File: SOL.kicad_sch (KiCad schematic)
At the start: 4 parts, among them J2 Conn_Coaxial, J3 Conn_Coaxial, J4 Conn_Coaxial

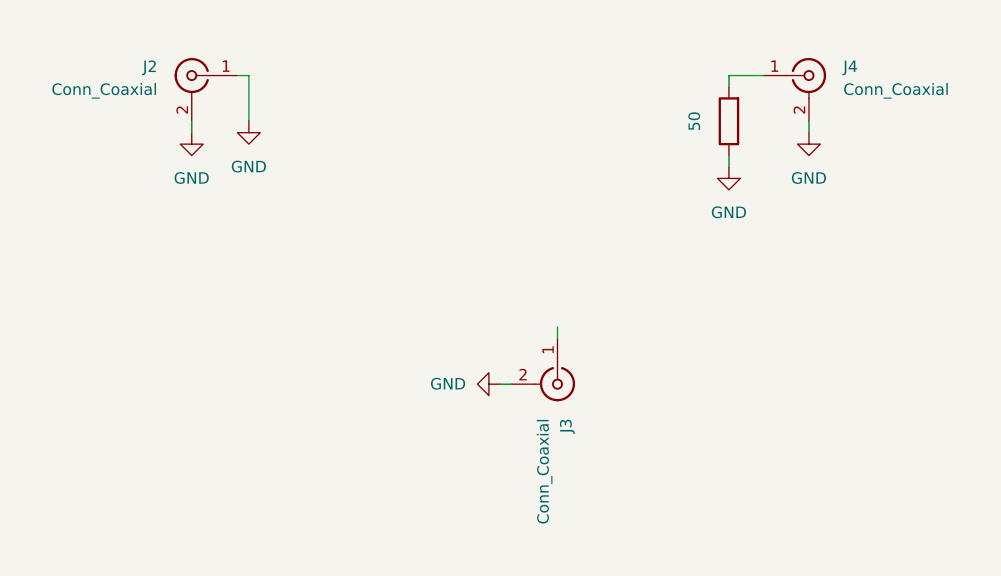
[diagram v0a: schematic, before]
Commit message: used altium files to build kicad models of mm5800 and started new twpatron
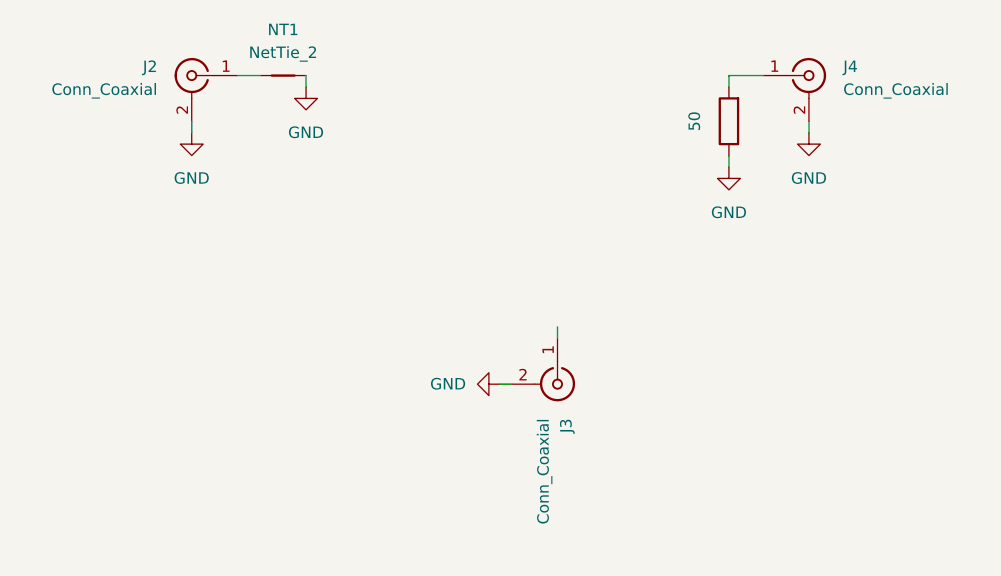
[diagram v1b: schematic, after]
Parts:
- added NT1: NetTie_2, Jumper:SolderJumper-2_P1.3mm_Bridged_Pad1.0x1.5mm, symbol Device:NetTie_2
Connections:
- net GND: now also NT1.2; no longer J2.1 (In)
- new net: J2.1 (In), NT1.1
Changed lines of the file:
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@@
 	(wire
 		(pts
-			(xy 97.79 73.66) (xy 97.79 78.74)
+			(xy 104.14 74.93) (xy 104.14 73.66)
 		)
 		(stroke
@@
 	(wire
 		(pts
-			(xy 96.52 73.66) (xy 97.79 73.66)
+			(xy 96.52 73.66) (xy 99.06 73.66)
 		)
 		(stroke
@@
 	)
 	(symbol
+		(lib_id "Device:NetTie_2")
+		(at 101.6 73.66 0)
+		(unit 1)
+		(exclude_from_sim no)
+		(in_bom no)
+		(on_board yes)
+		(dnp no)
+		(fields_autoplaced yes)
+		(property "Reference" "NT1"
+			(at 101.6 68.58 0)
+			(effects
+				(font
+					(size 1.27 1.27)
+				)
+			)
+		)
+		(property "Value" "NetTie_2"
+			(at 101.6 71.12 0)
+			(effects
+				(font
+					(size 1.27 1.27)
+				)
+			)
+		)
+		(property "Footprint" "Jumper:SolderJumper-2_P1.3mm_Bridged_Pad1.0x1.5mm"
+			(at 101.6 73.66 0)
+			(effects
+				(font
+					(size 1.27 1.27)
+				)
+				(hide yes)
+			)
+		)
+		(property "Datasheet" "~"
+			(at 101.6 73.66 0)
+			(effects
+				(font
+					(size 1.27 1.27)
+				)
+				(hide yes)
+			)
+		)
+		(property "Description" "Net tie, 2 pins"
+			(at 101.6 73.66 0)
+			(effects
+				(font
+					(size 1.27 1.27)
+				)
+				(hide yes)
+			)
+		)
+		(pin "2"
+		)
+		(pin "1"
+		)
+		(instances
+			(project ""
+				(path "/27633a03-897e-4d8a-8472-386b3ffbd891"
+					(reference "NT1")
+					(unit 1)
+				)
+			)
+		)
+	)
+	(symbol
 		(lib_id "power:GND")
-		(at 97.79 78.74 0)
+		(at 104.14 74.93 0)
 		(unit 1)
 		(exclude_from_sim no)
@@
 		(fields_autoplaced yes)
 		(property "Reference" "#PWR08"
-			(at 97.79 85.09 0)
+			(at 104.14 81.28 0)
 			(effects
 				(font
@@
 		)
 		(property "Value" "GND"
-			(at 97.79 83.82 0)
+			(at 104.14 80.01 0)
 			(effects
 				(font
@@
 		)
 		(property "Footprint" ""
-			(at 97.79 78.74 0)
+			(at 104.14 74.93 0)
 			(effects
 				(font
@@
 		)
 		(property "Datasheet" ""
-			(at 97.79 78.74 0)
+			(at 104.14 74.93 0)
 			(effects
 				(font
@@
 		)
 		(property "Description" "Power symbol creates a global label with name \"GND\" , ground"
-			(at 97.79 78.74 0)
-			(effects
-				(font
+			(at 104.14 74.93 0)
+			(effects
+				(font
